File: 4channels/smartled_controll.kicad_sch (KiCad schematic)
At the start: 102 parts, among them J1 Conn_01x04, J2 Conn_01x02, SW1 SW_Push, U1 OC5028B, U2 MAX485E, U3 PY32F003F1xUx, U4 OC5864, U5 SGM2033-3.3, U6 OC5028B, U7 GS8521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

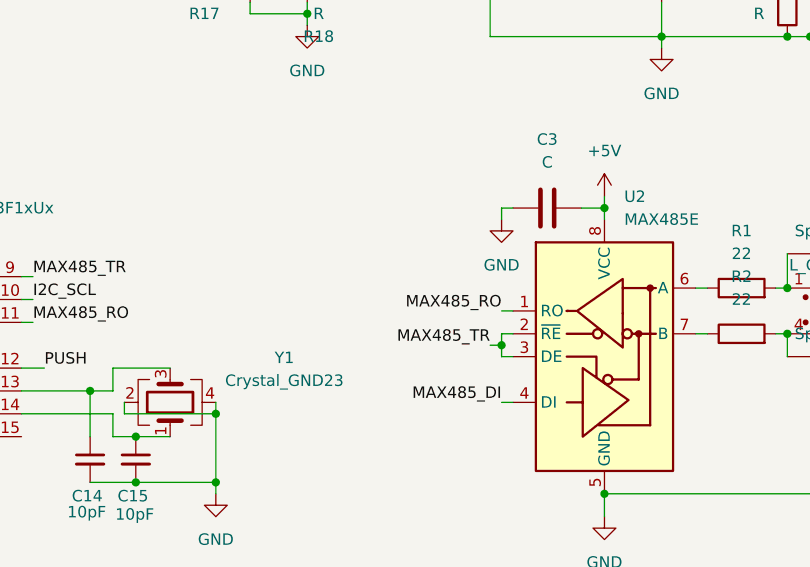
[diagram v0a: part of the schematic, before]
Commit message: MAX485 RO添加稳压二极管做电平转换
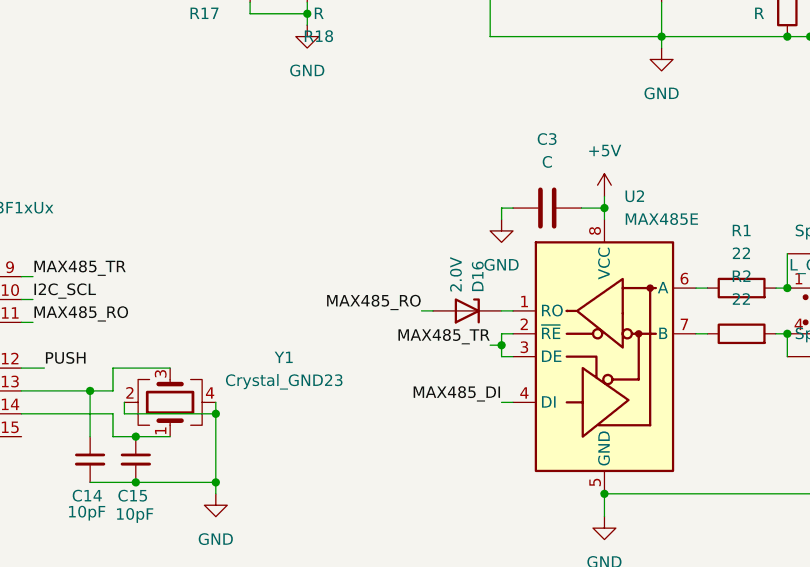
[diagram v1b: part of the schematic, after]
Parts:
- added D16: 2.0V, Diode_SMD:D_SOD-523, symbol Device:D_Zener
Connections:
- net MAX485_RO: now also D16.2 (A); no longer U2.1 (RO)
- new net: D16.1 (K), U2.1 (RO)
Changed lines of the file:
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@@
 	(wire
 		(pts
+			(xy 161.29 82.55) (xy 162.56 82.55)
+		)
+		(stroke
+			(width 0)
+			(type default)
+		)
+	)
+	(wire
+		(pts
 			(xy 217.17 85.09) (xy 209.55 85.09)
 		)
@@
 	(wire
 		(pts
-			(xy 161.29 82.55) (xy 162.56 82.55)
+			(xy 152.4 82.55) (xy 153.67 82.55)
 		)
 		(stroke
@@
 	)
 	(label "MAX485_RO"
-		(at 161.29 82.55 180)
+		(at 152.4 82.55 180)
 		(effects
 			(font
@@
 					(unit 1)
 				)
+			)
+		)
+	)
+	(symbol
+		(lib_id "Device:D_Zener")
+		(at 157.48 82.55 0)
+		(mirror y)
+		(unit 1)
+		(exclude_from_sim no)
+		(in_bom yes)
+		(on_board yes)
+		(dnp no)
+		(property "Reference" "D16"
+			(at 158.6922 80.518 90)
+			(effects
+				(font
+					(size 1.27 1.27)
+				)
+				(justify left)
+			)
+		)
+		(property "Value" "2.0V"
+			(at 156.2679 80.518 90)
+			(effects
+				(font
+					(size 1.27 1.27)
+				)
+				(justify left)
+			)
+		)
+		(property "Footprint" "Diode_SMD:D_SOD-523"
+			(at 157.48 82.55 0)
+			(effects
+				(font
+					(size 1.27 1.27)
+				)
+				(hide yes)
+			)
+		)
+		(property "Datasheet" "~"
+			(at 157.48 82.55 0)
+			(effects
+				(font
+					(size 1.27 1.27)
+				)
+				(hide yes)
+			)
+		)
+		(property "Description" "Zener diode"
+			(at 157.48 82.55 0)
+			(effects
+				(font
+					(size 1.27 1.27)
+				)
+				(hide yes)
+			)
+		)
+		(pin "1"
+		)
+		(pin "2"
+		)
+		(instances
+			(project "smartled_controll"
+				(path "/b299fa7e-4ddc-4ca9-9929-510e6cf892c6"
+					(reference "D16")
+					(unit 1)
+				)
